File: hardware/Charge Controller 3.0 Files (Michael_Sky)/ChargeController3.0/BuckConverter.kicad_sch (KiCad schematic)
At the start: 27 parts, among them Q5 AONS66614, Q6 AONS66614, Q7 AONS66614, Q8 AONS66614

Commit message: New formatting
New formatting
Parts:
- C12, C13, C17, C18, C2, C24: footprint Capacitor_SMD:C_0201_0603Metric -> bmsfootprints:CAP_UCD_6P3X7P7_NCH
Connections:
- net SOL renamed IN
- net SYS/BATT renamed OUT
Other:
- moved on the sheet: C14, C15, C16

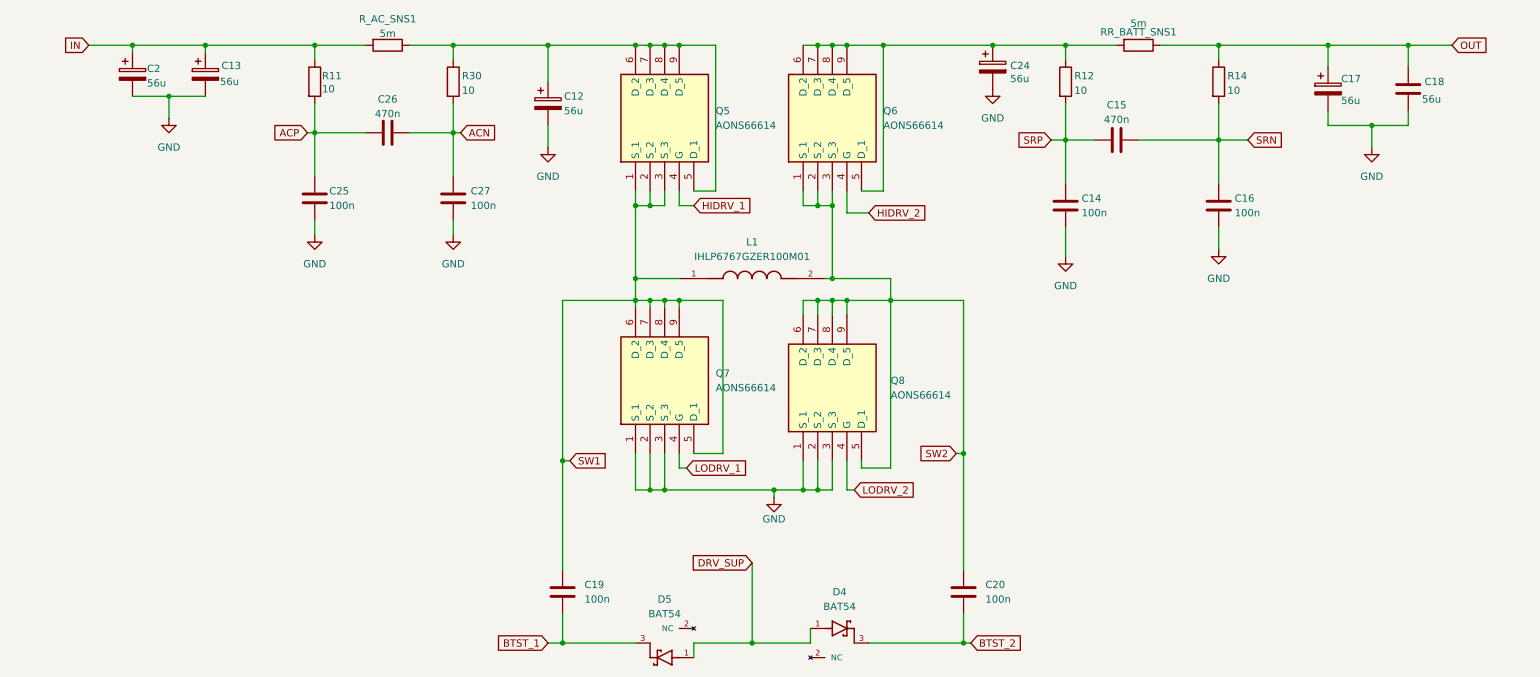
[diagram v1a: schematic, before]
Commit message: Final PCB?
inhibits rework, filtering rework
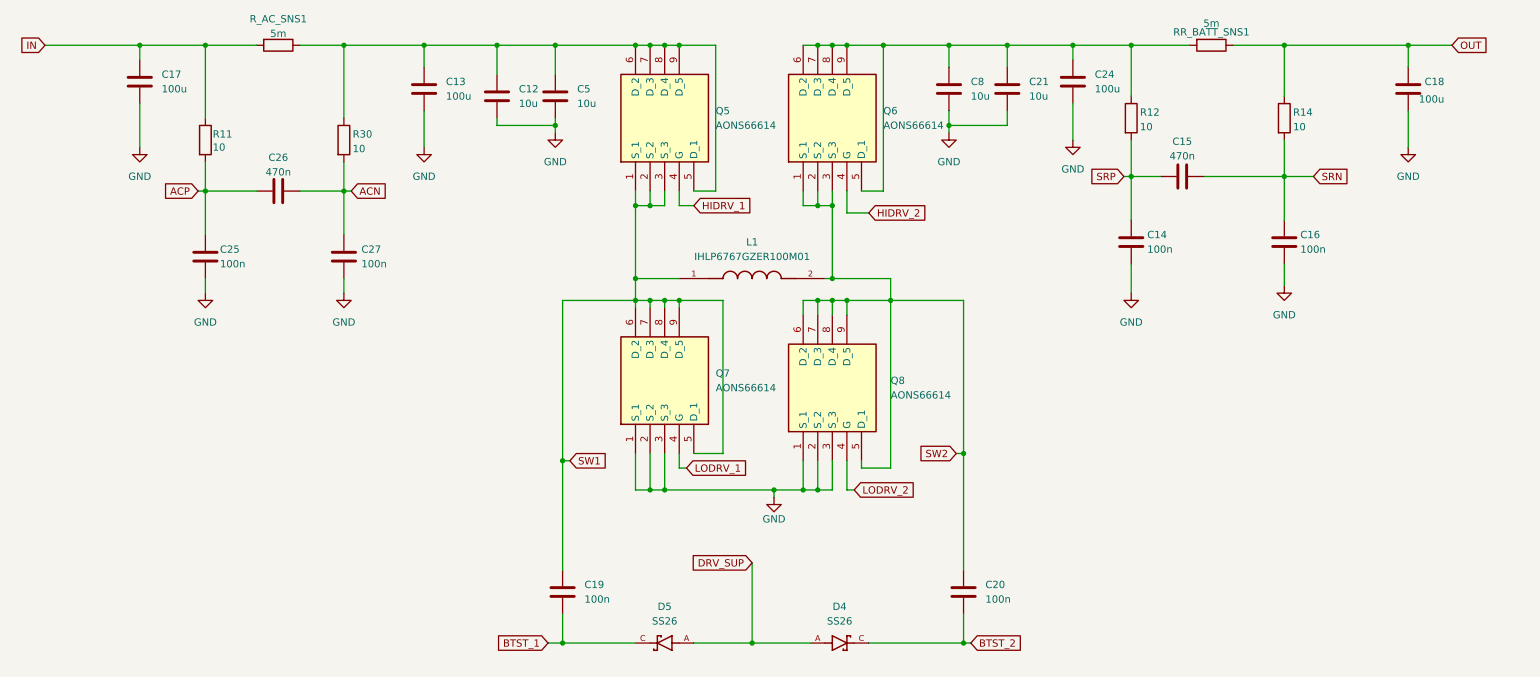
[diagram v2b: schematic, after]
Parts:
- removed C12, C13, C17, C2, C24: 56u, bmsfootprints:CAP_UCD_6P3X7P7_NCH, symbol Device:C_Polarized
- removed D4, D5: BAT54, bmsfootprints:BAT54, symbol BAT54:BAT54
- added C12, C21, C5, C8: 10u, bmsfootprints:CGA6P1X7R1N106K250AC, symbol Device:C
- added C13, C17, C24: 100u, bmsfootprints:T520D107, symbol Device:C
- added D4, D5: SS26, bmsfootprints:SS26, symbol SS26:SS26
- C18: value 56u -> 100u; footprint bmsfootprints:CAP_UCD_6P3X7P7_NCH -> bmsfootprints:T520D107
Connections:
- net BTST_1: now also D5.C
- net BTST_2: now also D4.C
- net DRV_SUP: now also D4.A, D5.A
- net GND: now also C12.2, C13.2, C17.2, C21.2, C24.2, C5.2, C8.2
- net IN: now also C17.1
- net at Q6.5 (D_1), Q6.6 (D_2), Q6.7 (D_3)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: now also C21.1, C24.1, C8.1
- net at Q5.5 (D_1), Q5.6 (D_2), Q5.7 (D_3)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: now also C12.1, C13.1, C5.1
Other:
- moved on the sheet: C14, C15, C16, C25, C26, C27, R11, R12, R14, R30, RR_BATT_SNS1, R_AC_SNS1
